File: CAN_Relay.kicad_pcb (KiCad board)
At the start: 2 copper layers, 41 parts, among them J1 430450601, J4 691305340008, J5 691305340008, U1 Teensy4.0, U2 BTS716GB, U3 BTS716GB, U4 ADM3057EBRWZ, U5 LM22676MRE-5.0/NOPB

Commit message: added smd pins for teensy
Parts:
- removed U1: Teensy4.0, teensy.pretty-master:Teensy40
- added J2: BCS-114-L-S-PE-BE, BCS:SAMTEC_BCS-114-L-S-PE-BE, F.Cu at (85.3, 88.7)
- added J3: BCS-114-L-S-PE-BE, BCS:SAMTEC_BCS-114-L-S-PE-BE, F.Cu at (85.2, 73.7)
- moved F1 86.6 mm to (129.7, 71.6), turned to 0 degrees
- moved U4 86.4 mm to (170.9, 85.3)
- moved R4 71.1 mm to (125.7, 78.7), turned to 90 degrees
- moved R3 68.3 mm to (125.6, 82.5), turned to -90 degrees
- moved D2 67.5 mm to (121.0, 82.8), turned to 180 degrees
- moved D1 62.7 mm to (121.0, 78.5), turned to 180 degrees
- moved C1 40.3 mm to (161.6, 75.1), turned to 90 degrees
- moved C6 39.5 mm to (163.6, 58.8)
- moved C7 39.5 mm to (163.6, 60.9)
- moved C2 34.9 mm to (164.2, 69.4), turned to 180 degrees
- moved C4 34.1 mm to (152.9, 57.7)
- moved C5 34.1 mm to (152.9, 60.7)
- moved L1 33.2 mm to (161.6, 70.9), turned to 90 degrees
- moved U3 31.6 mm to (96.0, 102.7)
- moved L2 30.1 mm to (165.0, 72.5), turned to 90 degrees
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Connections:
- U2 pad 7: Net-(U1-2_OUT2) -> unconnected-(U2-IN3-Pad7)
- U2 pad 8: Net-(U1-1_TX1_CTX2_MISO1) -> unconnected-(U2-ST3/4-Pad8)
- U2 pad 9: Net-(U1-0_RX1_CRX2_CS1) -> unconnected-(U2-IN4-Pad9)
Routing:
- net GND: track 136.1 -> 92.7 mm
- net Net-(D6-K): track 19.4 -> 0.00 mm
- net Net-(D7-K): track 18.6 -> 0.00 mm
- net Net-(D10-K): track 17.6 -> 0.00 mm
- net Net-(D3-K): track 17.5 -> 0.00 mm
- net Net-(D5-K): track 14.1 -> 0.00 mm
- net Net-(D4-K): track 13.8 -> 0.00 mm
- net Net-(D8-K): track 13.5 -> 0.00 mm
- net Net-(D9-K): track 12.5 -> 0.00 mm
- net Net-(F1-Pad2): track 0.00 -> 7.94 mm
- net +12: track 22.2 -> 18.4 mm

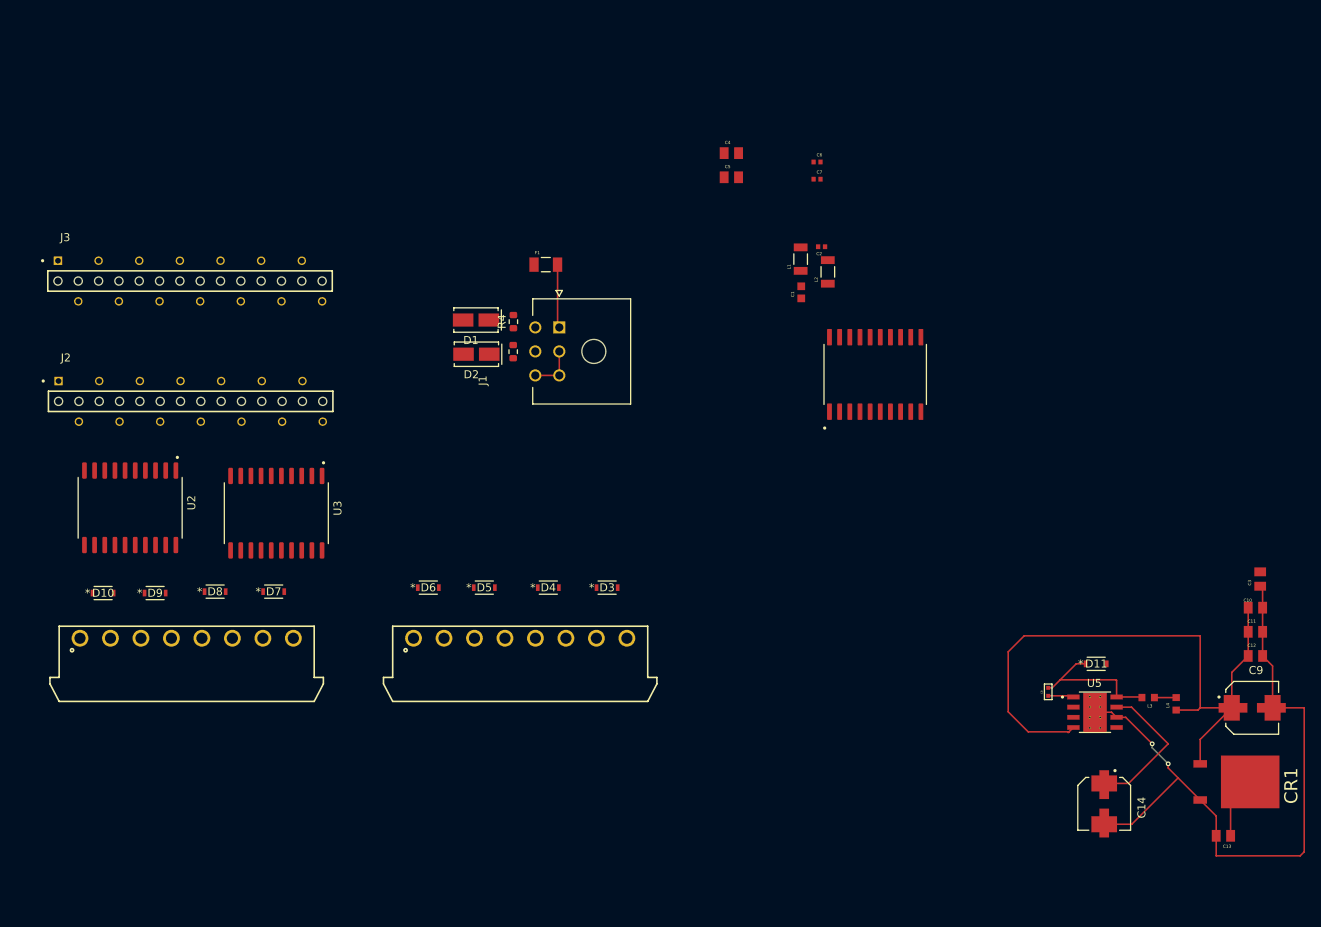
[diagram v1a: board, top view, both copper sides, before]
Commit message: wired all but relay outputs
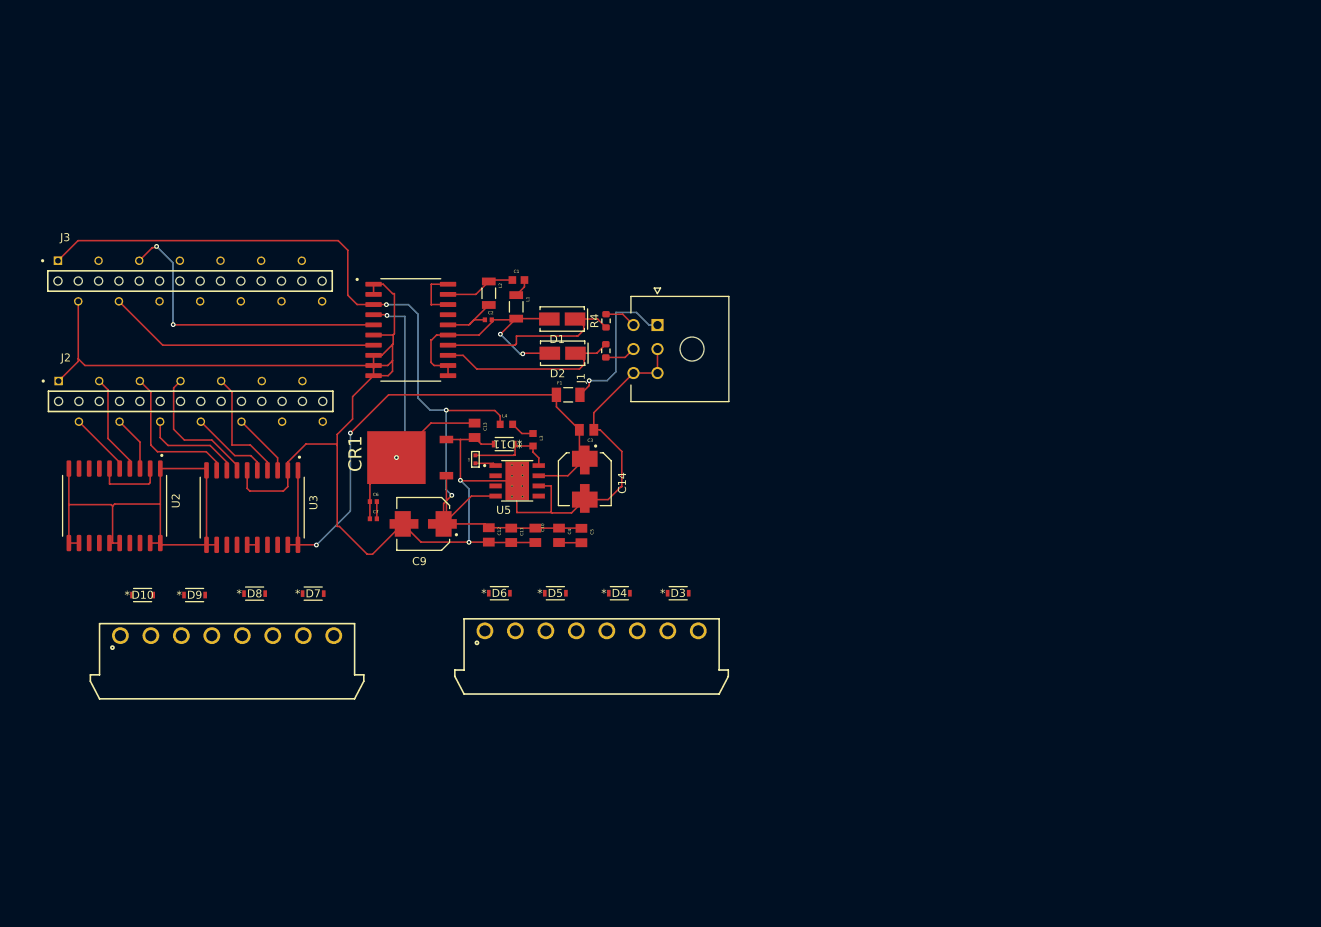
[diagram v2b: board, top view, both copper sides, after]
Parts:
- moved CR1 113.9 mm to (111.2, 95.7), turned to 90 degrees
- moved C13 106.4 mm to (120.8, 92.3), turned to -90 degrees
- moved C9 106.1 mm to (114.4, 104.0), turned to 180 degrees
- moved C12 97.0 mm to (122.6, 105.4), turned to -90 degrees
- moved C11 93.8 mm to (125.4, 105.4), turned to -90 degrees
- moved L4 90.7 mm to (124.8, 91.6), turned to 0 degrees
- moved C10 90.5 mm to (128.4, 105.4), turned to -90 degrees
- moved C3 86.2 mm to (134.8, 92.2), turned to 180 degrees
- moved L3 83.4 mm to (128.1, 93.5), turned to -90 degrees
- moved D11 78.9 mm to (124.5, 94.0), turned to 180 degrees
- moved U5 77.8 mm to (126.1, 98.6)
- moved C8 77.3 mm to (120.9, 95.9)
- moved C14 76.6 mm to (134.6, 98.4)
- moved C7 69.8 mm to (108.1, 103.4)
- moved C6 69.8 mm to (108.1, 101.2)
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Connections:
- J3 pad 01: +5V -> +5
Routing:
- net GND: track 92.7 -> 217.9 mm
- net +12: track 18.4 -> 134.8 mm, vias 0 -> 2
- net +5: track 79.9 -> 122.4 mm, vias 0 -> 3
- net /CANRX: track 0.00 -> 38.6 mm, vias 0 -> 2
- net +3.3: track 7.75 -> 42.7 mm, vias 0 -> 2
- net /CANTX: track 0.00 -> 34.1 mm
- net /GNDCan: track 0.00 -> 32.5 mm, vias 0 -> 2
- net /CaNHi: track 0.00 -> 24.6 mm
- net /CaNLi: track 0.00 -> 24.2 mm
- net Net-(U3-IN4): track 0.00 -> 18.7 mm
- net Net-(U3-IN3): track 0.00 -> 16.8 mm
- net Net-(U3-ST1/2): track 0.00 -> 14.9 mm
- net Net-(U3-ST3/4): track 0.00 -> 12.6 mm
- net Net-(U2-ST1/2): track 0.00 -> 12.5 mm
- net Net-(F1-Pad2): track 7.94 -> 19.6 mm, vias 0 -> 1
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
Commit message: Complete with Errors
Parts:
- moved D7 29.9 mm to (70.7, 113.1), turned to 180 degrees
- moved D3 23.7 mm to (123.0, 117.7), turned to 180 degrees
- moved D6 22.3 mm to (145.6, 117.7), turned to 180 degrees
- moved D8 17.5 mm to (75.8, 112.7), turned to 180 degrees
- moved D4 9.84 mm to (130.5, 117.8), turned to 180 degrees
- moved D10 8.90 mm to (88.2, 112.8), turned to 180 degrees
- moved D5 8.78 mm to (138.0, 117.8), turned to 180 degrees
- moved J4 7.17 mm to (85.2, 123.4)
- moved J5 5.67 mm to (134.4, 123.0)
- moved D9 2.75 mm to (83.1, 112.9), turned to 180 degrees
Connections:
- J4 pad 1: Net-(D10-K) -> GND
- J4 pad 2: GND -> Net-(D7-K)
- J4 pad 3: Net-(D9-K) -> GND
- J4 pad 4: GND -> Net-(D8-K)
- J4 pad 5: Net-(D8-K) -> GND
- J4 pad 6: GND -> Net-(D9-K)
- J4 pad 7: Net-(D7-K) -> GND
- J4 pad 8: GND -> Net-(D10-K)
- J5 pad 1: Net-(D6-K) -> GND
- J5 pad 2: GND -> Net-(D3-K)
- J5 pad 3: Net-(D5-K) -> GND
- J5 pad 4: GND -> Net-(D4-K)
- J5 pad 5: Net-(D4-K) -> GND
- J5 pad 6: GND -> Net-(D5-K)
- J5 pad 7: Net-(D3-K) -> GND
- J5 pad 8: GND -> Net-(D6-K)
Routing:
- net GND: track 217.9 -> 418.8 mm, vias 2 -> 3
- net Net-(D6-K): track 0.00 -> 63.4 mm
- net Net-(D5-K): track 0.00 -> 57.2 mm
- net Net-(D4-K): track 0.00 -> 53.2 mm
- net Net-(D3-K): track 0.00 -> 46.7 mm
- net Net-(D10-K): track 0.00 -> 33.7 mm
- net Net-(D9-K): track 0.00 -> 25.3 mm
- net Net-(D8-K): track 0.00 -> 20.9 mm
- net Net-(D7-K): track 0.00 -> 18.6 mm
- net +12: track 134.8 -> 149.6 mm
- net /GNDCanx: track 9.10 -> 18.1 mm

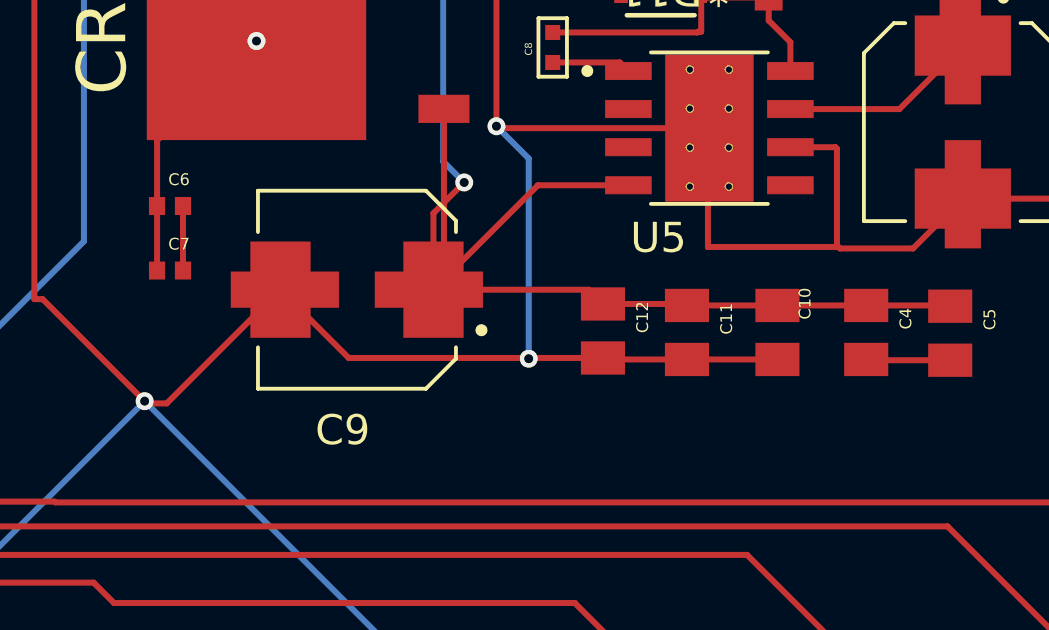
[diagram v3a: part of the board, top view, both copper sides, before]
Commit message: fixed trace not being ground
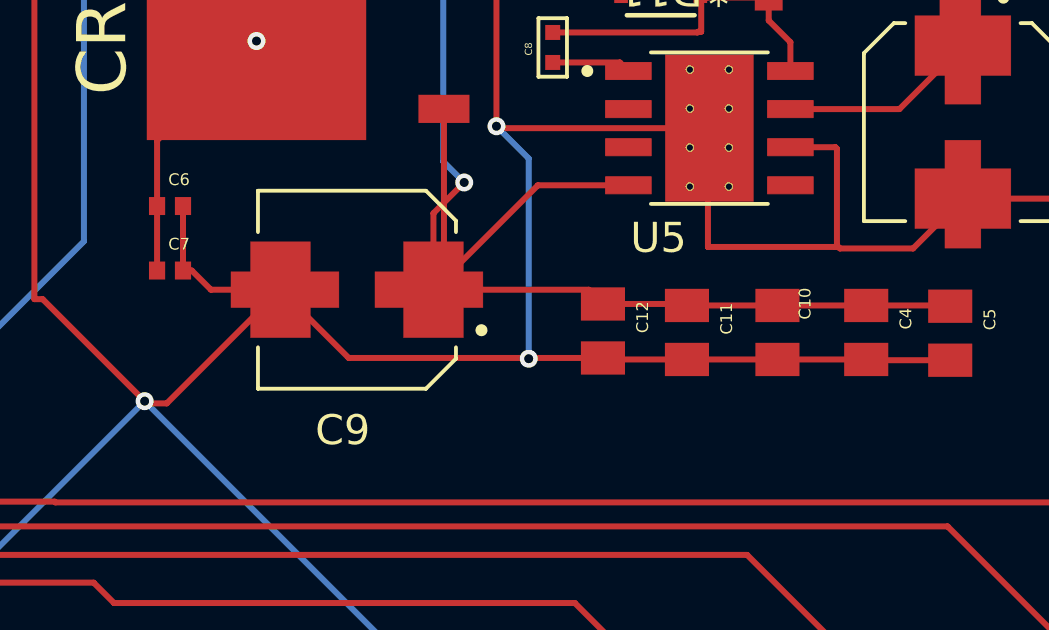
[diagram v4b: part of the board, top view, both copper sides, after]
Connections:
- C4 pad 2: Net-(C4-Pad2) -> GND
- C5 pad 2: Net-(C4-Pad2) -> GND
- C6 pad 2: Net-(C4-Pad2) -> GND
- C7 pad 2: Net-(C4-Pad2) -> GND
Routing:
- net GND: track 418.8 -> 430.2 mm
- net Net-(C4-Pad2): track 4.96 -> 0.00 mm

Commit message: experimented with ground and power planes
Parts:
- moved C13 7.75 mm to (113.3, 90.4), turned to 0 degrees
- moved D9 2.00 mm to (81.1, 112.6)
- moved F1 1.96 mm to (134.4, 88.3)
- moved U5 0.99 mm to (125.9, 99.6)
- moved C1 0.50 mm to (126.2, 73.0)
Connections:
- U2 pad 2: Net-(U2-GND1/2) -> GND
- U2 pad 6: Net-(U2-GND1/2) -> GND
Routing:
- net GND: track 430.2 -> 32.8 mm, vias 3 -> 37
- net +12: track 149.6 -> 33.5 mm, vias 2 -> 16
- net +5: track 122.4 -> 47.3 mm, vias 3 -> 0
- net +3.3: track 42.7 -> 9.02 mm, vias 2 -> 0
- net Net-(U2-GND1/2): track 8.84 -> 0.00 mm
- net Net-(D10-K): track 33.7 -> 29.1 mm
- net /CANRX: track 38.6 -> 34.2 mm, vias 2 -> 0
- net Net-(D6-K): track 63.4 -> 59.1 mm
- net /CaNH: track 4.01 -> 0.00 mm
- net /CaNL: track 3.89 -> 0.00 mm
- net /VCC50CAN: track 8.23 -> 10.6 mm
- net Net-(D9-K): track 25.3 -> 23.3 mm
- net Net-(F1-Pad2): track 19.6 -> 21.5 mm, vias 1 -> 0
- net /GNDCanx: track 18.1 -> 16.3 mm
- net Net-(D5-K): track 57.2 -> 58.4 mm
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- added copper zone on B.Cu, net +12
- added copper zone on F.Cu, net +12
- added copper zone on F.Cu, net +5
- added copper zone on B.Cu, net GND
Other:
- board outline added: 91.4 x 66 mm

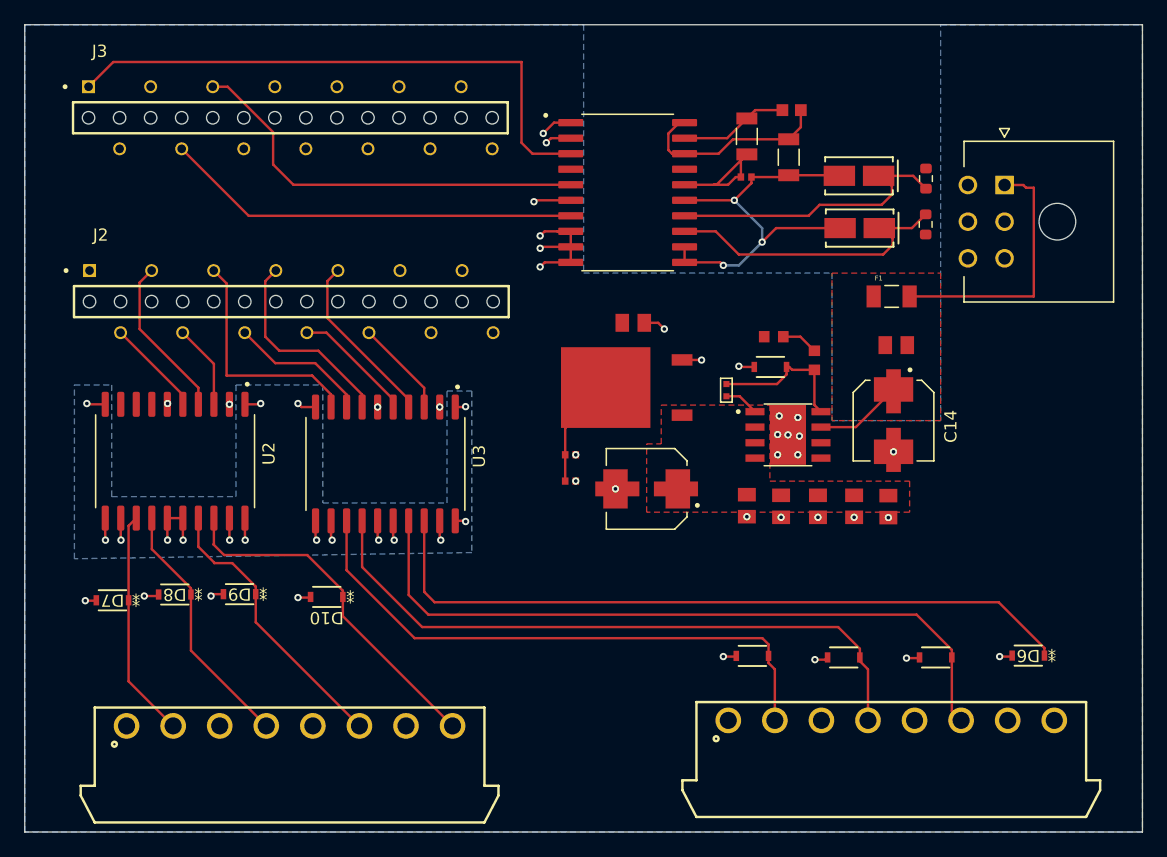
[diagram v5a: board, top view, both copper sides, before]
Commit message: No errors, but I hate the PCB layout
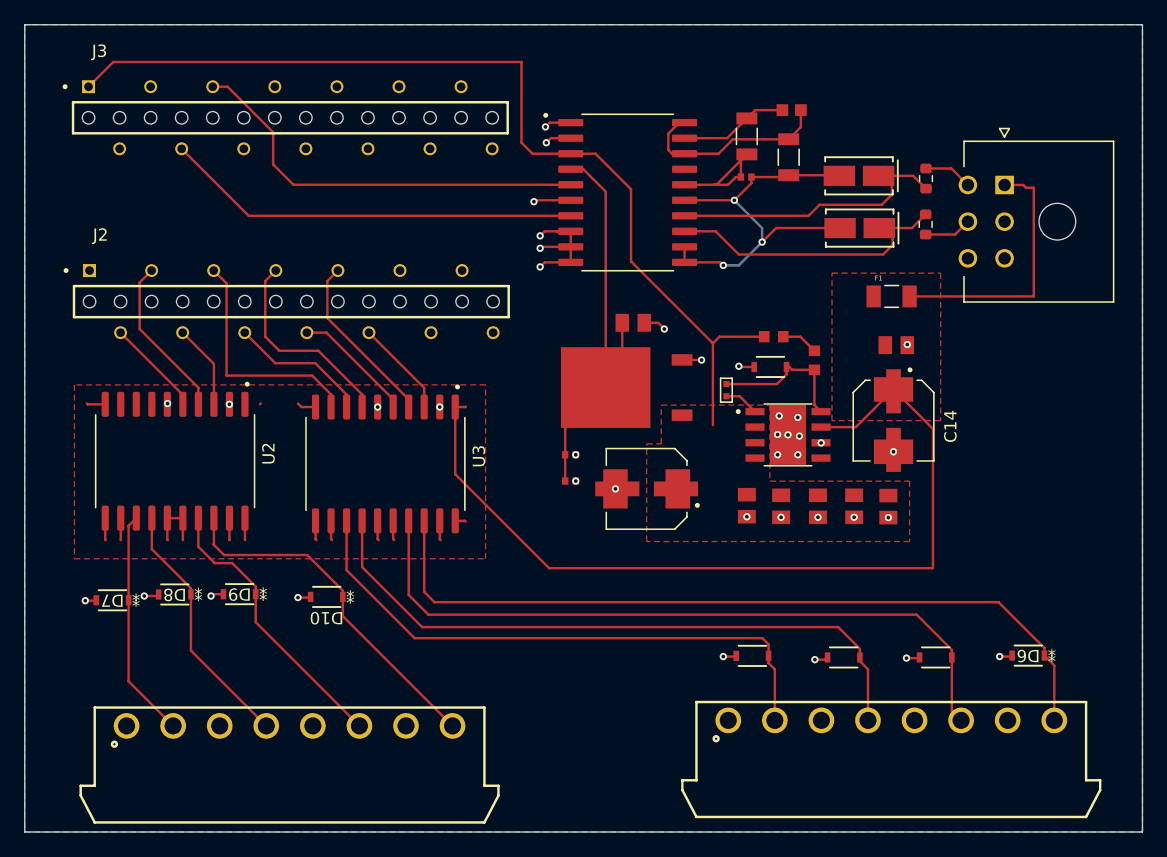
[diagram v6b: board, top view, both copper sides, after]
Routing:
- net +12: track 33.5 -> 96.0 mm, vias 16 -> 0
- net +5: track 47.3 -> 79.9 mm
- net +3.3: track 9.02 -> 34.5 mm
- net Net-(D6-K): track 59.1 -> 64.7 mm
- net /CaNH: track 0.00 -> 3.99 mm
- net /CaNL: track 0.00 -> 3.89 mm
- net GND: track 32.8 -> 32.5 mm, vias 37 -> 39
- removed copper zone on B.Cu, net +12
